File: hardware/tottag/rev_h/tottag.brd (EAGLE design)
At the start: 68.1 x 39.6 mm, 216 parts, among them J1 USB4110-GF-A, J2 DM3AT-SF-PEJM5, J3 TC2030-JLINK-NL-2SIDE, J4 TC2030-JLINK-NL-2SIDE, J5 MOLEX-PICO-SPOX-3SIDE, Q1 CSD75207W15, Q2 CSD75207W15, T1 HHM1595A1, U1 DW1000, U10 STM32F091CC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

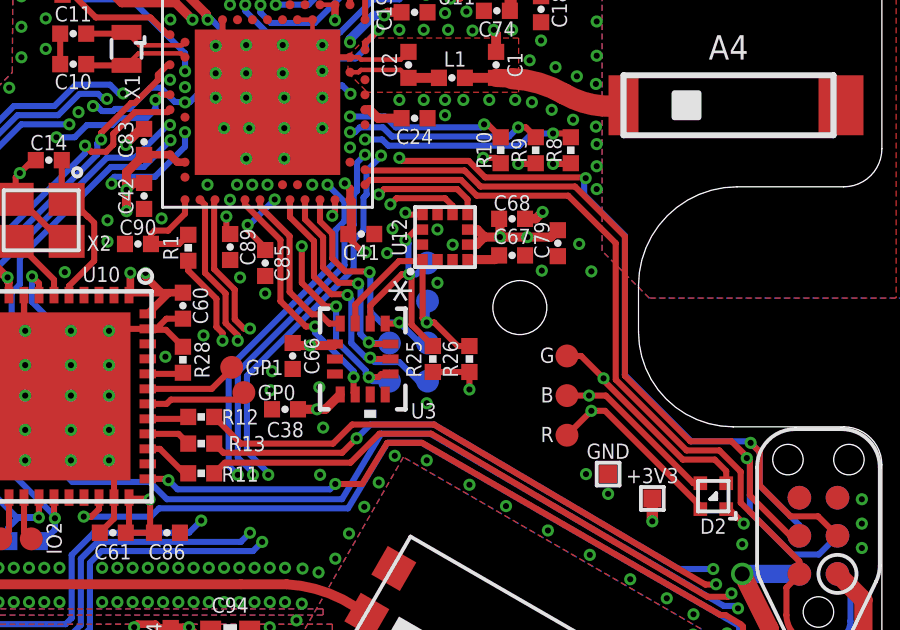
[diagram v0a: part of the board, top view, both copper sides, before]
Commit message: rev_h: wire mag DRDY to 6dof MRDRY pin
*now* this connection makes sense to me
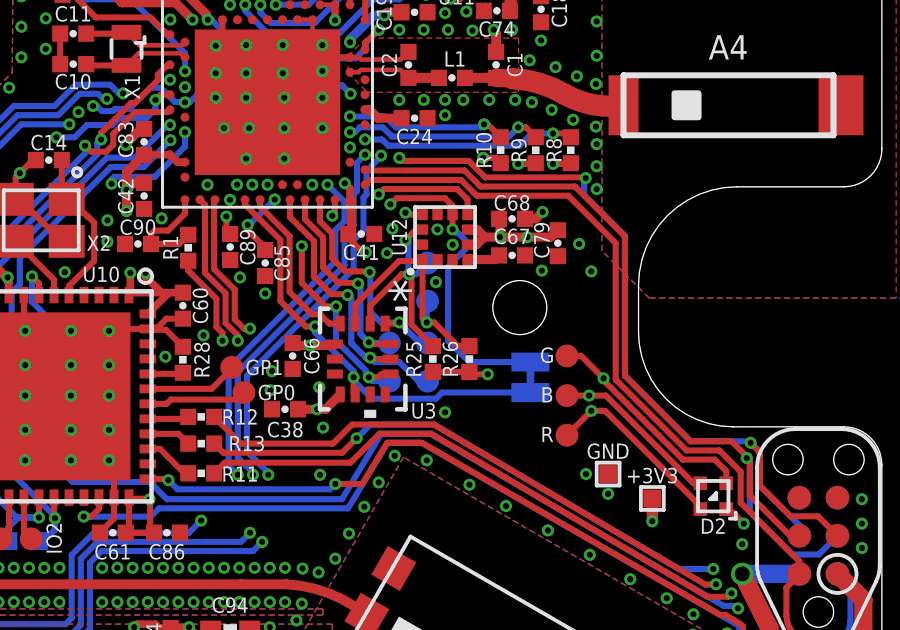
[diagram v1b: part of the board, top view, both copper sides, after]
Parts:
- added JP4: JUMPER-SMT_2_NC_TRACE_SILK, SparkFun-Jumpers:SMT-JUMPER_2_NC_TRACE_SILK
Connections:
- net MAG_DRDY: now also JP4.1
- net NRF_IMU_INT2: now also JP4.2
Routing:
- net MAG_DRDY: track 5.22 -> 12.9 mm, vias 2 -> 3
- net NRF_IMU_INT2: track 8.19 -> 14.5 mm
- added copper zone on layer 15, net N$23
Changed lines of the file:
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@@
 </layers>
 <board>
-<fusionsync huburn="a.YnVzaW5lc3M6dWNzZDc1OA" projecturn="a.YnVzaW5lc3M6dWNzZDc1OCMyMDIwMDUzMDMwMzI4NTUyNg" f3durn="urn:adsk.wipprod:dm.lineage:rzUGj1kvRPCORpM7Y38XuQ" pcbguid="" lastpulledtime="" lastsyncedchangeguid="" latestrevisionid="75524250-0e8d-4369-9e0b-1fb55c241ce6" lastsyncedrevisionid="75524250-0e8d-4369-9e0b-1fb55c241ce6" lastboardhashguid="853535db-d5ca-ae5b-083e-0a8cd8f7d9ee" lastpushedtime="2021-02-16T20:55:19Z" linktopcb3d="true"/>
+<fusionsync huburn="a.YnVzaW5lc3M6dWNzZDc1OA" projecturn="a.YnVzaW5lc3M6dWNzZDc1OCMyMDIwMDUzMDMwMzI4NTUyNg" f3durn="urn:adsk.wipprod:dm.lineage:rzUGj1kvRPCORpM7Y38XuQ" pcbguid="" lastpulledtime="" lastsyncedchangeguid="" latestrevisionid="46348900-6281-48db-9099-0236c059d8c9" lastsyncedrevisionid="46348900-6281-48db-9099-0236c059d8c9" lastboardhashguid="a03f274f-d729-ae65-c9cb-e0d60f56228a" lastpushedtime="2021-02-18T14:12:14Z" linktopcb3d="true"/>
 <plain>
 <text x="32.1564" y="2.032" size="1.016" layer="21" font="vector" ratio="12" align="top-center">nRF</text>
@@
 <element name="TP28" library="headers" package="PAD.03X.03" value="TEST-POINT" x="18.923" y="13.716" smashed="yes" rot="MR0"/>
 <element name="TP29" library="headers" package="PAD.03X.03" value="TEST-POINT" x="18.923" y="14.986" smashed="yes" rot="MR0"/>
+<element name="JP4" library="SparkFun-Jumpers" library_urn="urn:adsk.eagle:library:528" package="SMT-JUMPER_2_NC_TRACE_SILK" package3d_urn="urn:adsk.eagle:package:39281/1" value="JUMPER-SMT_2_NC_TRACE_SILK" x="22.352" y="11.176" smashed="yes" rot="MR270">
+<attribute name="NAME" x="22.352" y="9.8298" size="0.6096" layer="26" font="vector" ratio="20" rot="MR180" align="bottom-center"/>
+<attribute name="VALUE" x="23.495" y="11.176" size="0.6096" layer="28" font="vector" ratio="20" rot="MR270" align="top-center"/>
+</element>
 </elements>
 <signals>
@@
 <via x="-13.4874" y="19.7104" extent="1-16" drill="0.2032"/>
 <via x="-14.097" y="9.0932" extent="1-16" drill="0.2032"/>
-<via x="19.2532" y="14.3256" extent="1-16" drill="0.2032"/>
+<via x="19.2024" y="14.351" extent="1-16" drill="0.2032"/>
 <via x="13.6906" y="10.7442" extent="1-16" drill="0.2032"/>
 <via x="13.7414" y="11.3792" extent="1-16" drill="0.2032"/>
@@
 <via x="19.7612" y="15.5956" extent="1-16" drill="0.2032"/>
 <via x="15.4432" y="9.4996" extent="1-16" drill="0.2032"/>
-<via x="18.8976" y="10.3124" extent="1-16" drill="0.2032"/>
+<via x="19.5072" y="10.0076" extent="1-16" drill="0.2032"/>
 <via x="23.9776" y="15.621" extent="1-16" drill="0.2032"/>
 <via x="15.3162" y="10.8458" extent="1-16" drill="0.2032"/>
@@
 <wire x1="16.4592" y1="11.3792" x2="15.17176875" y2="12.66663125" width="0.2032" layer="16"/>
 <wire x1="15.17176875" y1="12.66663125" x2="15.17176875" y2="12.86983125" width="0.2032" layer="16"/>
+<contactref element="JP4" pad="2"/>
+<wire x1="22.352" y1="10.668" x2="19.4056" y2="10.668" width="0.2032" layer="16"/>
+<wire x1="19.4056" y1="10.668" x2="19.2024" y2="10.4648" width="0.2032" layer="16"/>
+<wire x1="17.0688" y1="10.4648" x2="16.4592" y2="11.0744" width="0.2032" layer="16"/>
+<wire x1="16.4592" y1="11.0744" x2="16.4592" y2="11.176" width="0.2032" layer="16"/>
+<wire x1="19.2024" y1="10.4648" x2="17.0688" y2="10.4648" width="0.2032" layer="16"/>
 </signal>
 <signal name="STM_INTERRUPT">
@@
 <via x="18.1864" y="16.6624" extent="1-16" drill="0.2032"/>
 <wire x1="19.1008" y1="11.35253125" x2="20.32" y2="11.35253125" width="0.2032" layer="1"/>
-<wire x1="20.32" y1="11.35253125" x2="20.32" y2="10.7696" width="0.2032" layer="1"/>
-<via x="20.32" y="10.7696" extent="1-16" drill="0.2032"/>
+<wire x1="20.32" y1="11.35253125" x2="20.39493125" y2="11.2776" width="0.2032" layer="1"/>
+<wire x1="20.9296" y1="11.2776" x2="20.39493125" y2="11.2776" width="0.2032" layer="1"/>
+<via x="20.9296" y="11.2776" extent="1-16" drill="0.2032"/>
 <wire x1="16.28013125" y1="15.9512" x2="16.28013125" y2="15.82546875" width="0.2032" layer="1"/>
 <wire x1="16.764" y1="15.3416" x2="16.28013125" y2="15.82546875" width="0.2032" layer="1"/>
@@
 <wire x1="19.5072" y1="17.145" x2="19.7572" y2="16.895" width="0.2032" layer="1"/>
 <wire x1="19.7572" y1="16.895" x2="19.7572" y2="16.5996" width="0.2032" layer="1"/>
+<contactref element="JP4" pad="1"/>
+<wire x1="19.7572" y1="16.5996" x2="19.7572" y2="16.1076" width="0.2032" layer="1"/>
+<wire x1="19.7572" y1="16.1076" x2="19.7612" y2="16.1036" width="0.2032" layer="1"/>
+<via x="19.7612" y="16.1036" extent="1-16" drill="0.2032"/>
+<wire x1="19.9295375" y1="16.002" x2="20.1676" y2="15.7639375" width="0.2032" layer="16"/>
+<wire x1="20.1676" y1="15.7639375" x2="20.1676" y2="15.4272625" width="0.2032" layer="16"/>
+<wire x1="19.7612" y1="16.1036" x2="19.8628" y2="16.002" width="0.2032" layer="16"/>
+<wire x1="19.8628" y1="16.002" x2="19.9295375" y2="16.002" width="0.2032" layer="16"/>
+<wire x1="20.1676" y1="15.4272625" x2="19.6088" y2="14.8684625" width="0.2032" layer="16"/>
+<wire x1="19.6088" y1="12.3952" x2="20.32" y2="11.684" width="0.2032" layer="16"/>
+<wire x1="19.6088" y1="14.8684625" x2="19.6088" y2="12.3952" width="0.2032" layer="16"/>
+<wire x1="20.32" y1="11.684" x2="22.352" y2="11.684" width="0.2032" layer="16"/>
+</signal>
+<signal name="N$23">
+<polygon width="0.2032" layer="15" pour="cutout">
+<vertex x="21.6408" y="11.3792"/>
+<vertex x="21.6408" y="10.9728"/>
+<vertex x="23.0632" y="10.9728"/>
+<vertex x="23.0632" y="11.3792"/>
+</polygon>
 </signal>
 </signals>

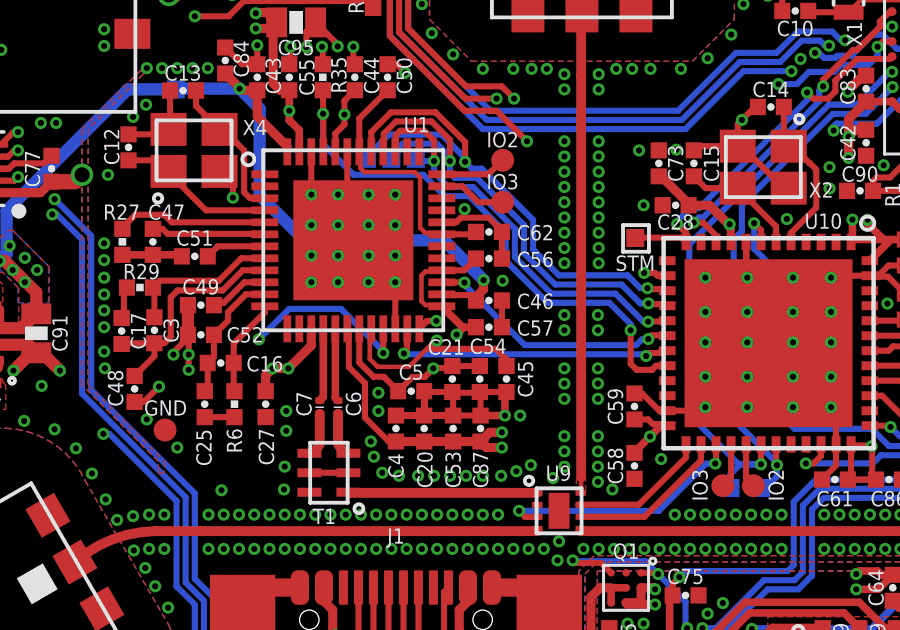
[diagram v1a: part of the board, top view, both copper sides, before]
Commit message: rev_h: add last missing test point
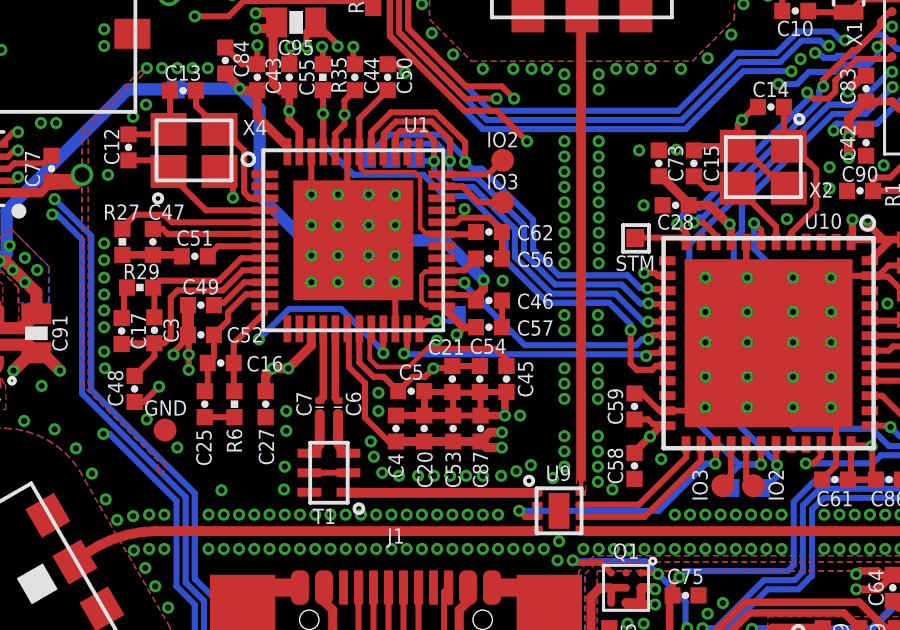
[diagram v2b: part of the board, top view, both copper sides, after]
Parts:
- added DW_SPI_CS: TPTP06SQ, testpad:TP06SQ
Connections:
- net !DW_SPI_CS: now also DW_SPI_CS.TP
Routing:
- net !DW_SPI_CS: track 9.08 -> 9.85 mm
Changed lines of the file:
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@@
 <text x="17.7546" y="13.4874" size="0.508" layer="22" font="vector" ratio="18" rot="MR180" align="top-center">SCL</text>
 <text x="17.7546" y="14.8082" size="0.508" layer="22" font="vector" ratio="18" rot="MR180" align="top-center">SDA</text>
+<wire x1="-4.572" y1="11.8618" x2="-4.572" y2="11.0744" width="0.127" layer="22"/>
+<wire x1="-3.7592" y1="11.8618" x2="-3.7592" y2="11.0744" width="0.127" layer="22"/>
+<wire x1="-4.572" y1="11.8872" x2="-3.7592" y2="11.8872" width="0.127" layer="22"/>
+<wire x1="-4.5466" y1="11.0744" x2="-3.7592" y2="11.0744" width="0.127" layer="22"/>
+<wire x1="-4.17123125" y1="16.130275" x2="-5.0464125" y2="17.132453125" width="0.127" layer="22"/>
 </plain>
 <attributes>
@@
 <attribute name="VALUE" x="23.495" y="11.176" size="0.6096" layer="28" font="vector" ratio="20" rot="MR270" align="top-center"/>
 </element>
+<element name="DW_SPI_CS" library="testpad" library_urn="urn:adsk.eagle:library:385" package="TP06SQ" package3d_urn="urn:adsk.eagle:package:27952/1" value="TPTP06SQ" x="-4.1656" y="11.4808" smashed="yes" rot="MR0">
+<attribute name="NAME" x="-4.3751" y="11.9936" size="0.508" layer="26" font="vector" ratio="18" rot="MR90"/>
+<attribute name="TP_SIGNAL_NAME" value="" x="-4.1656" y="9.5758" size="1" layer="38" rot="MR0"/>
+<attribute name="VALUE" x="-3.9116" y="11.0998" size="0.0254" layer="28" rot="MR0"/>
+</element>
 </elements>
 <signals>
@@
 <wire x1="-3.4798" y1="11.2844" x2="-2.877" y2="11.8872" width="0.2032" layer="15"/>
 <wire x1="-2.877" y1="11.8872" x2="1.05790625" y2="11.8872" width="0.2032" layer="15"/>
+<contactref element="DW_SPI_CS" pad="TP"/>
+<wire x1="-4.1656" y1="11.4808" x2="-4.362" y2="11.2844" width="0.1524" layer="16"/>
+<wire x1="-4.362" y1="11.2844" x2="-4.8514" y2="11.2844" width="0.1524" layer="16"/>
 </signal>
 <signal name="DW_SPI_CLK">

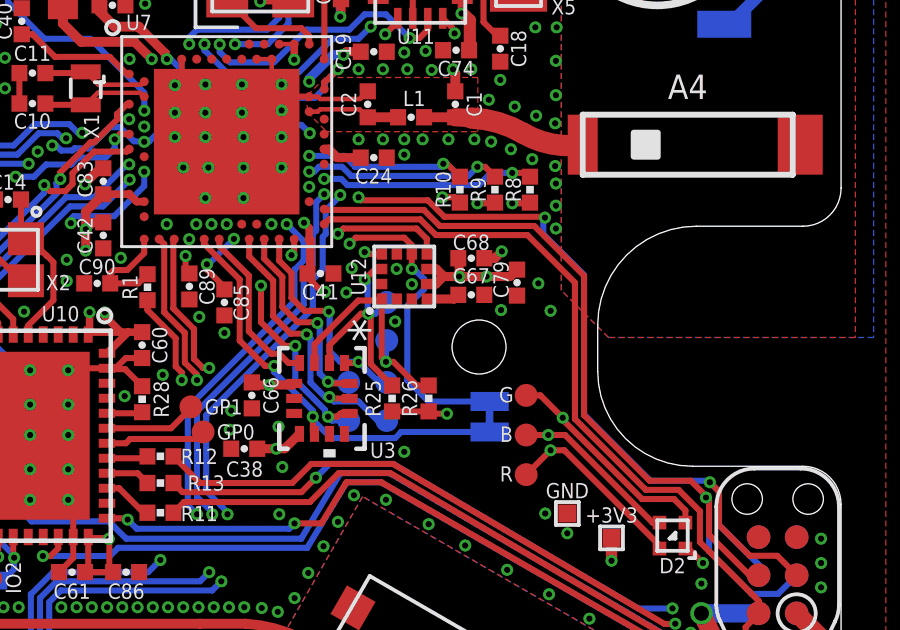
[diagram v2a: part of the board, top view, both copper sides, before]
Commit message: rev_h: fix cap routing for magnetometer
The VddIO pin was connected to the filter/decap network of Vdd,
rather than directly to the Vdd plane as proscribed in the datasheet.
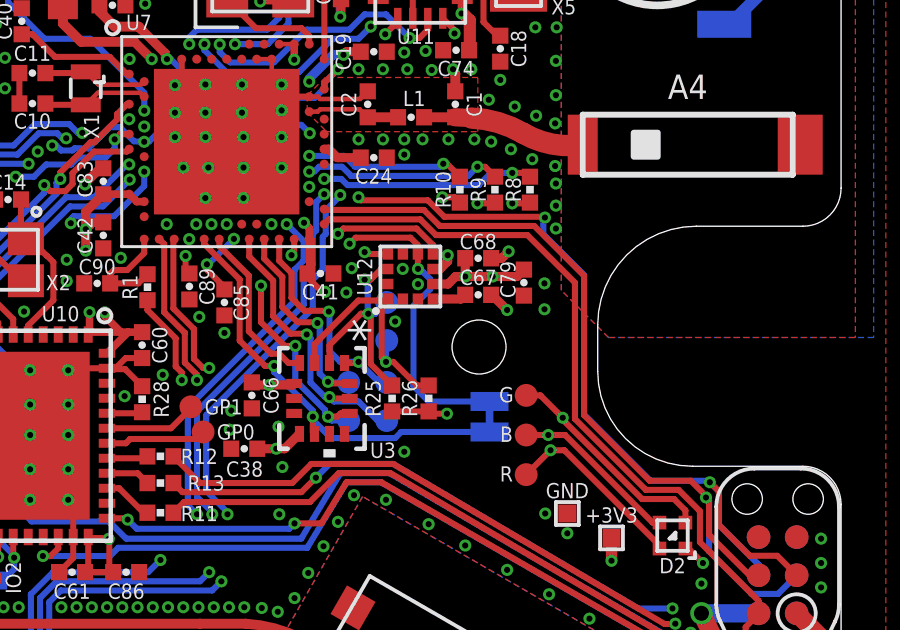
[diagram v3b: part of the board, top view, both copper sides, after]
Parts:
- moved C67 0.23 mm to (22.0, 15.2)
- moved C68 0.23 mm to (22.0, 16.5)
- moved C79 0.23 mm to (23.5, 15.6)
- moved U12 0.20 mm to (19.7, 15.8)
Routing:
- net GND: track 189.7 -> 190.5 mm
- net +3V3: track 165.8 -> 166.1 mm, vias 54 -> 55
